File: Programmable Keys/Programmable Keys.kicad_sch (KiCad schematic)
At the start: 18 parts

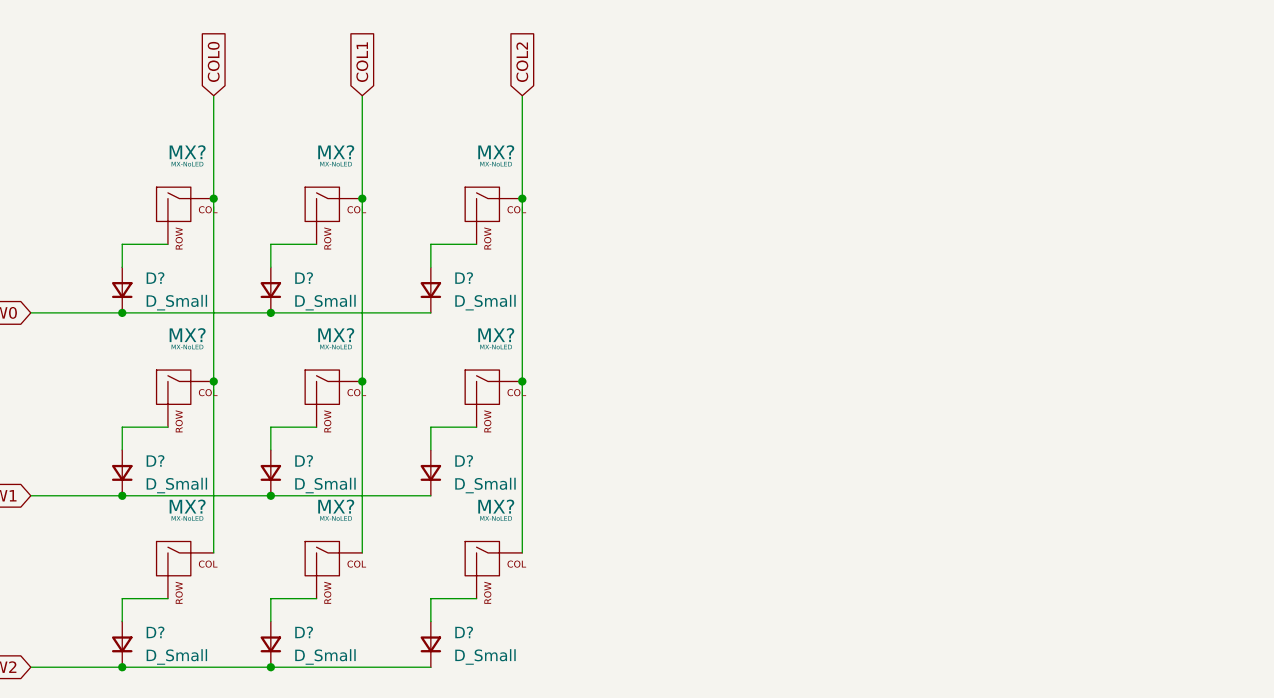
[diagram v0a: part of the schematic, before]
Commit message: Added connectors, labeled keys
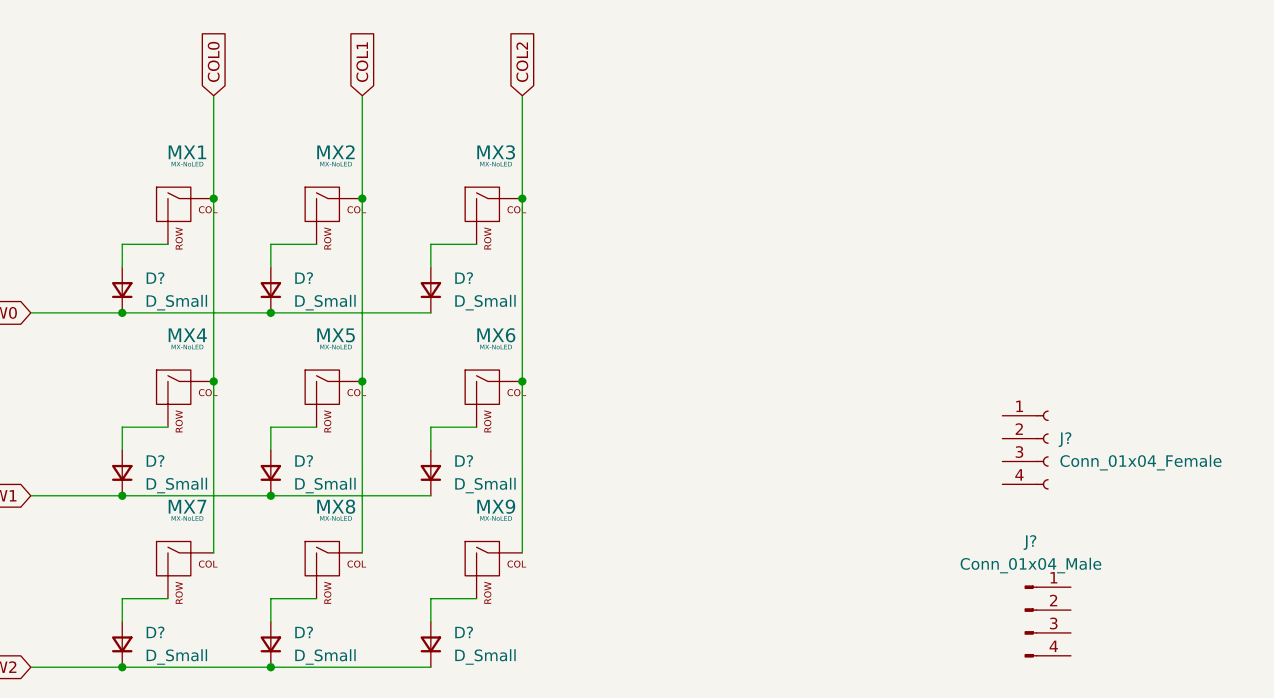
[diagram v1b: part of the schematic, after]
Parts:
- added J?: Conn_01x04_Female, symbol Connector:Conn_01x04_Female
- added J?: Conn_01x04_Male, symbol Connector:Conn_01x04_Male
- gave numbers to parts that had none: 9
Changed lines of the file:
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@@
   (symbol (lib_id "MX_Alps_Hybrid:MX-NoLED") (at 127 36.83 0) (unit 1)
     (in_bom yes) (on_board yes) (fields_autoplaced)
-    (property "Reference" "MX?" (id 0) (at 127.8856 30.48 0)
+    (property "Reference" "MX3" (id 0) (at 127.8856 30.48 0)
       (effects (font (size 1.524 1.524)))
     )
@@
   (symbol (lib_id "MX_Alps_Hybrid:MX-NoLED") (at 127 57.15 0) (unit 1)
     (in_bom yes) (on_board yes) (fields_autoplaced)
-    (property "Reference" "MX?" (id 0) (at 127.8856 50.8 0)
+    (property "Reference" "MX6" (id 0) (at 127.8856 50.8 0)
       (effects (font (size 1.524 1.524)))
     )
@@
   (symbol (lib_id "MX_Alps_Hybrid:MX-NoLED") (at 127 76.2 0) (unit 1)
     (in_bom yes) (on_board yes) (fields_autoplaced)
-    (property "Reference" "MX?" (id 0) (at 127.8856 69.85 0)
+    (property "Reference" "MX9" (id 0) (at 127.8856 69.85 0)
       (effects (font (size 1.524 1.524)))
     )
@@
   (symbol (lib_id "MX_Alps_Hybrid:MX-NoLED") (at 92.71 76.2 0) (unit 1)
     (in_bom yes) (on_board yes) (fields_autoplaced)
-    (property "Reference" "MX?" (id 0) (at 93.5956 69.85 0)
+    (property "Reference" "MX7" (id 0) (at 93.5956 69.85 0)
       (effects (font (size 1.524 1.524)))
     )
@@
     (pin "2")
   )
+  (symbol (lib_id "Connector:Conn_01x04_Female") (at 189.23 62.23 0) (unit 1)
+    (in_bom yes) (on_board yes) (fields_autoplaced)
+    (property "Reference" "J?" (id 0) (at 190.5 62.2299 0)
+      (effects (font (size 1.27 1.27)) (justify left))
+    )
+    (property "Value" "Conn_01x04_Female" (id 1) (at 190.5 64.7699 0)
+      (effects (font (size 1.27 1.27)) (justify left))
+    )
+    (property "Footprint" "" (id 2) (at 189.23 62.23 0)
+      (effects (font (size 1.27 1.27)) hide)
+    )
+    (property "Datasheet" "~" (id 3) (at 189.23 62.23 0)
+      (effects (font (size 1.27 1.27)) hide)
+    )
+    (pin "1")
+    (pin "2")
+    (pin "3")
+    (pin "4")
+  )
   (symbol (lib_id "Device:D_Small") (at 120.65 45.72 90) (unit 1)
     (in_bom yes) (on_board yes) (fields_autoplaced)
@@
   (symbol (lib_id "MX_Alps_Hybrid:MX-NoLED") (at 109.22 36.83 0) (unit 1)
     (in_bom yes) (on_board yes) (fields_autoplaced)
-    (property "Reference" "MX?" (id 0) (at 110.1056 30.48 0)
+    (property "Reference" "MX2" (id 0) (at 110.1056 30.48 0)
       (effects (font (size 1.524 1.524)))
     )
@@
     (pin "2")
   )
+  (symbol (lib_id "Connector:Conn_01x04_Male") (at 186.69 81.28 0) (unit 1)
+    (in_bom yes) (on_board yes) (fields_autoplaced)
+    (property "Reference" "J?" (id 0) (at 187.325 73.66 0))
+    (property "Value" "Conn_01x04_Male" (id 1) (at 187.325 76.2 0))
+    (property "Footprint" "" (id 2) (at 186.69 81.28 0)
+      (effects (font (size 1.27 1.27)) hide)
+    )
+    (property "Datasheet" "~" (id 3) (at 186.69 81.28 0)
+      (effects (font (size 1.27 1.27)) hide)
+    )
+    (pin "1")
+    (pin "2")
+    (pin "3")
+    (pin "4")
+  )
   (symbol (lib_id "MX_Alps_Hybrid:MX-NoLED") (at 92.71 57.15 0) (unit 1)
     (in_bom yes) (on_board yes) (fields_autoplaced)
-    (property "Reference" "MX?" (id 0) (at 93.5956 50.8 0)
+    (property "Reference" "MX4" (id 0) (at 93.5956 50.8 0)
       (effects (font (size 1.524 1.524)))
     )
@@
   (symbol (lib_id "MX_Alps_Hybrid:MX-NoLED") (at 109.22 76.2 0) (unit 1)
     (in_bom yes) (on_board yes) (fields_autoplaced)
-    (property "Reference" "MX?" (id 0) (at 110.1056 69.85 0)
+    (property "Reference" "MX8" (id 0) (at 110.1056 69.85 0)
       (effects (font (size 1.524 1.524)))
     )
@@
   (symbol (lib_id "MX_Alps_Hybrid:MX-NoLED") (at 109.22 57.15 0) (unit 1)
     (in_bom yes) (on_board yes) (fields_autoplaced)
-    (property "Reference" "MX?" (id 0) (at 110.1056 50.8 0)
+    (property "Reference" "MX5" (id 0) (at 110.1056 50.8 0)
       (effects (font (size 1.524 1.524)))
     )
@@
   (symbol (lib_id "MX_Alps_Hybrid:MX-NoLED") (at 92.71 36.83 0) (unit 1)
     (in_bom yes) (on_board yes) (fields_autoplaced)
-    (property "Reference" "MX?" (id 0) (at 93.5956 30.48 0)
+    (property "Reference" "MX1" (id 0) (at 93.5956 30.48 0)
       (effects (font (size 1.524 1.524)))
     )
@@
       (reference "D?") (unit 1) (value "D_Small") (footprint "")
     )
+    (path "/6bd1febb-4938-4c6c-97c8-f57b8767fbc9"
+      (reference "J?") (unit 1) (value "Conn_01x04_Female") (footprint "")
+    )
+    (path "/a0f37c66-2074-4f38-9287-5c1e7d61b568"
+      (reference "J?") (unit 1) (value "Conn_01x04_Male") (footprint "")
+    )
+    (path "/f15ab00c-943c-484a-b23d-b1b628e3d8b4"
+      (reference "MX1") (unit 1) (value "MX-NoLED") (footprint "")
+    )
+    (path "/89048221-4cd2-4088-9129-786c72d84035"
+      (reference "MX2") (unit 1) (value "MX-NoLED") (footprint "")
+    )
     (path "/0910a061-29f6-43fe-ada4-8b46e5ac764d"
-      (reference "MX?") (unit 1) (value "MX-NoLED") (footprint "")
+      (reference "MX3") (unit 1) (value "MX-NoLED") (footprint "")
+    )
+    (path "/a1e262c4-50ec-48e3-b461-95a8aea22533"
+      (reference "MX4") (unit 1) (value "MX-NoLED") (footprint "")
+    )
+    (path "/e61c1027-a0c0-427e-92d9-4c3d1848e11b"
+      (reference "MX5") (unit 1) (value "MX-NoLED") (footprint "")
     )
     (path "/0be1f922-df52-4384-8644-fba195e49916"
-      (reference "MX?") (unit 1) (value "MX-NoLED") (footprint "")
+      (reference "MX6") (unit 1) (value "MX-NoLED") (footprint "")
+    )
+    (path "/4b105a84-591f-48a6-a43e-639e102c54a9"
+      (reference "MX7") (unit 1) (value "MX-NoLED") (footprint "")
+    )
+    (path "/b299d47d-4b90-41c1-b81e-504a59e300a0"
+      (reference "MX8") (unit 1) (value "MX-NoLED") (footprint "")
     )
     (path "/17e7cec1-a749-4fd4-b8d0-f8db4961c65e"
-      (reference "MX?") (unit 1) (value "MX-NoLED") (footprint "")
-    )
-    (path "/4b105a84-591f-48a6-a43e-639e102c54a9"
-      (reference "MX?") (unit 1) (value "MX-NoLED") (footprint "")
-    )
-    (path "/89048221-4cd2-4088-9129-786c72d84035"
-      (reference "MX?") (unit 1) (value "MX-NoLED") (footprint "")
-    )
-    (path "/a1e262c4-50ec-48e3-b461-95a8aea22533"
-      (reference "MX?") (unit 1) (value "MX-NoLED") (footprint "")
-    )
-    (path "/b299d47d-4b90-41c1-b81e-504a59e300a0"
-      (reference "MX?") (unit 1) (value "MX-NoLED") (footprint "")
-    )
-    (path "/e61c1027-a0c0-427e-92d9-4c3d1848e11b"
-      (reference "MX?") (unit 1) (value "MX-NoLED") (footprint "")
-    )
-    (path "/f15ab00c-943c-484a-b23d-b1b628e3d8b4"
-      (reference "MX?") (unit 1) (value "MX-NoLED") (footprint "")
-    )
-  )
+      (reference "MX9") (unit 1) (value "MX-NoLED") (footprint "")
+    )
+  )

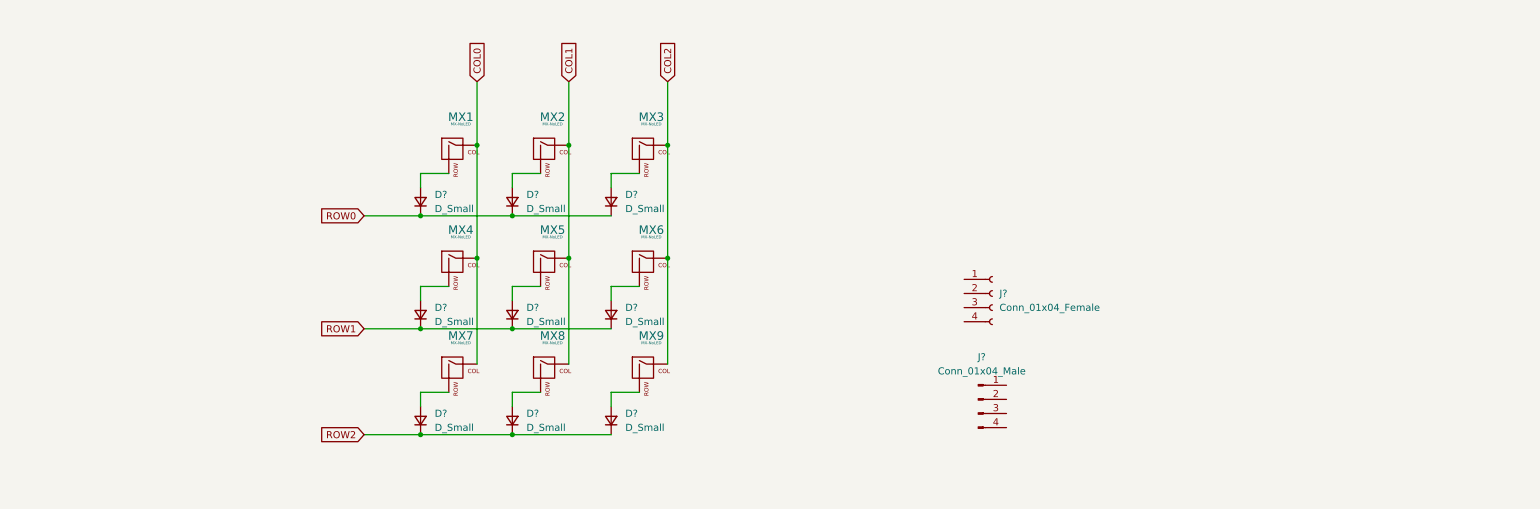
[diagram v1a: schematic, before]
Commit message: Added connectors, assigned footprints
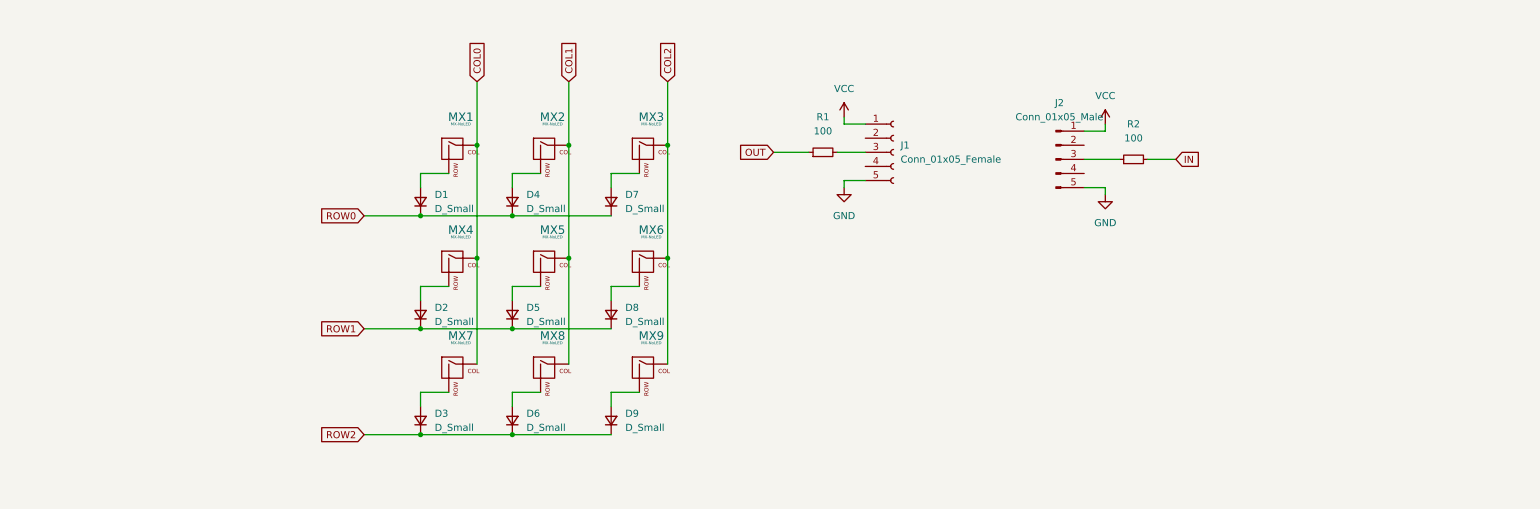
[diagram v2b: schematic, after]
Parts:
- removed J?: Conn_01x04_Female, symbol Connector:Conn_01x04_Female
- removed J?: Conn_01x04_Male, symbol Connector:Conn_01x04_Male
- added J1: Conn_01x05_Female, Connector_JST:JST_PH_B5B-PH-K_1x05_P2.00mm_Vertical, symbol Connector:Conn_01x05_Female
- added J2: Conn_01x05_Male, Connector_JST:JST_PH_B5B-PH-K_1x05_P2.00mm_Vertical, symbol Connector:Conn_01x05_Male
- added R1, R2: 100, Resistor_SMD:R_0805_2012Metric, symbol Device:R_Small
- D1, D2, D3, D4, D5, D6, D7, D8, D9: renamed from D?; footprint (none) -> Diode_SMD:D_SOD-123
- MX1, MX2, MX3, MX4, MX5, MX6, MX7, MX8, MX9: footprint (none) -> MX_Alps_Hybrid:MX-1U-NoLED
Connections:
- new net: J2.3 (Pin_3), R2.1
- new net: J1.3 (Pin_3), R1.2
- new net GND: J1.5 (Pin_5), J2.5 (Pin_5)
- new net IN: R2.2
- new net OUT: R1.1
- new net VCC: J1.1 (Pin_1), J2.1 (Pin_1)

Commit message: Updated connectors
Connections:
- net VCC: now also J1.2 (Pin_2), J2.2 (Pin_2)
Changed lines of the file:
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@@
+    (stroke (width 0) (type default) (color 0 0 0 0))
+  )
+  (wire (pts (xy 218.44 35.56) (xy 205.74 35.56))
     (stroke (width 0) (type default) (color 0 0 0 0))
   )
@@
     (stroke (width 0) (type default) (color 0 0 0 0))
   )
+  (wire (pts (xy 154.94 33.02) (xy 154.94 34.29))
+    (stroke (width 0) (type default) (color 0 0 0 0))
+  )
+  (wire (pts (xy 218.44 34.29) (xy 218.44 35.56))
+    (stroke (width 0) (type default) (color 0 0 0 0))
+  )
   (wire (pts (xy 217.17 38.1) (xy 222.25 38.1))
     (stroke (width 0) (type default) (color 0 0 0 0))
@@
   )
   (wire (pts (xy 107.95 80.01) (xy 102.87 80.01))
+    (stroke (width 0) (type default) (color 0 0 0 0))
+  )
+  (wire (pts (xy 154.94 34.29) (xy 166.37 34.29))
     (stroke (width 0) (type default) (color 0 0 0 0))
   )
@@
     (pin "2")
   )
+  (symbol (lib_id "power:VCC") (at 218.44 34.29 0) (unit 1)
+    (in_bom yes) (on_board yes) (fields_autoplaced)
+    (property "Reference" "#PWR0104" (id 0) (at 218.44 38.1 0)
+      (effects (font (size 1.27 1.27)) hide)
+    )
+    (property "Value" "VCC" (id 1) (at 218.44 29.21 0))
+    (property "Footprint" "" (id 2) (at 218.44 34.29 0)
+      (effects (font (size 1.27 1.27)) hide)
+    )
+    (property "Datasheet" "" (id 3) (at 218.44 34.29 0)
+      (effects (font (size 1.27 1.27)) hide)
+    )
+    (pin "1")
+  )
+  (symbol (lib_id "power:VCC") (at 162.56 30.48 0) (unit 1)
+    (in_bom yes) (on_board yes) (fields_autoplaced)
+    (property "Reference" "#PWR?" (id 0) (at 162.56 34.29 0)
+      (effects (font (size 1.27 1.27)) hide)
+    )
+    (property "Value" "VCC" (id 1) (at 162.56 25.4 0))
+    (property "Footprint" "" (id 2) (at 162.56 30.48 0)
+      (effects (font (size 1.27 1.27)) hide)
+    )
+    (property "Datasheet" "" (id 3) (at 162.56 30.48 0)
+      (effects (font (size 1.27 1.27)) hide)
+    )
+    (pin "1")
+  )
+  (symbol (lib_id "Device:D_Small") (at 120.65 45.72 90) (unit 1)
+    (in_bom yes) (on_board yes) (fields_autoplaced)
+    (property "Reference" "D7" (id 0) (at 123.19 44.4499 90)
+      (effects (font (size 1.27 1.27)) (justify right))
+    )
+    (property "Value" "D_Small" (id 1) (at 123.19 46.9899 90)
+      (effects (font (size 1.27 1.27)) (justify right))
+    )
+    (property "Footprint" "Diode_SMD:D_SOD-123" (id 2) (at 120.65 45.72 90)
+      (effects (font (size 1.27 1.27)) hide)
+    )
+    (property "Datasheet" "~" (id 3) (at 120.65 45.72 90)
+      (effects (font (size 1.27 1.27)) hide)
+    )
+    (pin "1")
+    (pin "2")
+  )
   (symbol (lib_id "power:VCC") (at 209.55 31.75 0) (unit 1)
     (in_bom yes) (on_board yes) (fields_autoplaced)
-    (property "Reference" "#PWR0104" (id 0) (at 209.55 35.56 0)
+    (property "Reference" "#PWR?" (id 0) (at 209.55 35.56 0)
       (effects (font (size 1.27 1.27)) hide)
     )
@@
     )
     (pin "1")
-  )
-  (symbol (lib_id "Device:D_Small") (at 120.65 45.72 90) (unit 1)
-    (in_bom yes) (on_board yes) (fields_autoplaced)
-    (property "Reference" "D7" (id 0) (at 123.19 44.4499 90)
-      (effects (font (size 1.27 1.27)) (justify right))
-    )
-    (property "Value" "D_Small" (id 1) (at 123.19 46.9899 90)
-      (effects (font (size 1.27 1.27)) (justify right))
-    )
-    (property "Footprint" "Diode_SMD:D_SOD-123" (id 2) (at 120.65 45.72 90)
-      (effects (font (size 1.27 1.27)) hide)
-    )
-    (property "Datasheet" "~" (id 3) (at 120.65 45.72 90)
-      (effects (font (size 1.27 1.27)) hide)
-    )
-    (pin "1")
-    (pin "2")
   )
   (symbol (lib_id "Device:D_Small") (at 120.65 66.04 90) (unit 1)
@@
     (pin "1")
   )
-  (symbol (lib_id "power:VCC") (at 162.56 30.48 0) (unit 1)
-    (in_bom yes) (on_board yes) (fields_autoplaced)
-    (property "Reference" "#PWR0103" (id 0) (at 162.56 34.29 0)
-      (effects (font (size 1.27 1.27)) hide)
-    )
-    (property "Value" "VCC" (id 1) (at 162.56 25.4 0))
-    (property "Footprint" "" (id 2) (at 162.56 30.48 0)
-      (effects (font (size 1.27 1.27)) hide)
-    )
-    (property "Datasheet" "" (id 3) (at 162.56 30.48 0)
+  (symbol (lib_id "power:VCC") (at 154.94 33.02 0) (unit 1)
+    (in_bom yes) (on_board yes) (fields_autoplaced)
+    (property "Reference" "#PWR0103" (id 0) (at 154.94 36.83 0)
+      (effects (font (size 1.27 1.27)) hide)
+    )
+    (property "Value" "VCC" (id 1) (at 154.94 27.94 0))
+    (property "Footprint" "" (id 2) (at 154.94 33.02 0)
+      (effects (font (size 1.27 1.27)) hide)
+    )
+    (property "Datasheet" "" (id 3) (at 154.94 33.02 0)
       (effects (font (size 1.27 1.27)) hide)
     )
@@
       (reference "#PWR0104") (unit 1) (value "VCC") (footprint "")
     )
+    (path "/6d1cfc32-67e5-4ae6-882b-693efde8f764"
+      (reference "#PWR?") (unit 1) (value "VCC") (footprint "")
+    )
+    (path "/80a9c8e3-2f25-4e61-9ec9-4d65b683dfb8"
+      (reference "#PWR?") (unit 1) (value "VCC") (footprint "")
+    )
     (path "/deaeb746-0d3d-4bb0-a186-8c685d641314"
